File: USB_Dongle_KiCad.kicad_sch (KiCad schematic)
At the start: 52 parts, among them J1 USB_C_Receptacle_USB2.0, J2 Conn SWD 02x05, J3 DM3BT-DSF-PEJS, SW1 PCM12SMTR, SW2 KMR223G LFG, U1 AMS1117-3.3, U2 STULPI01A, U3 USBULC6-2M6, U4 ESDA14V2-2BF3, U5 STM32F730R8Tx, Y1 3225 SMD Oscillator, Y2 24MHz / 10pF / 20ppm

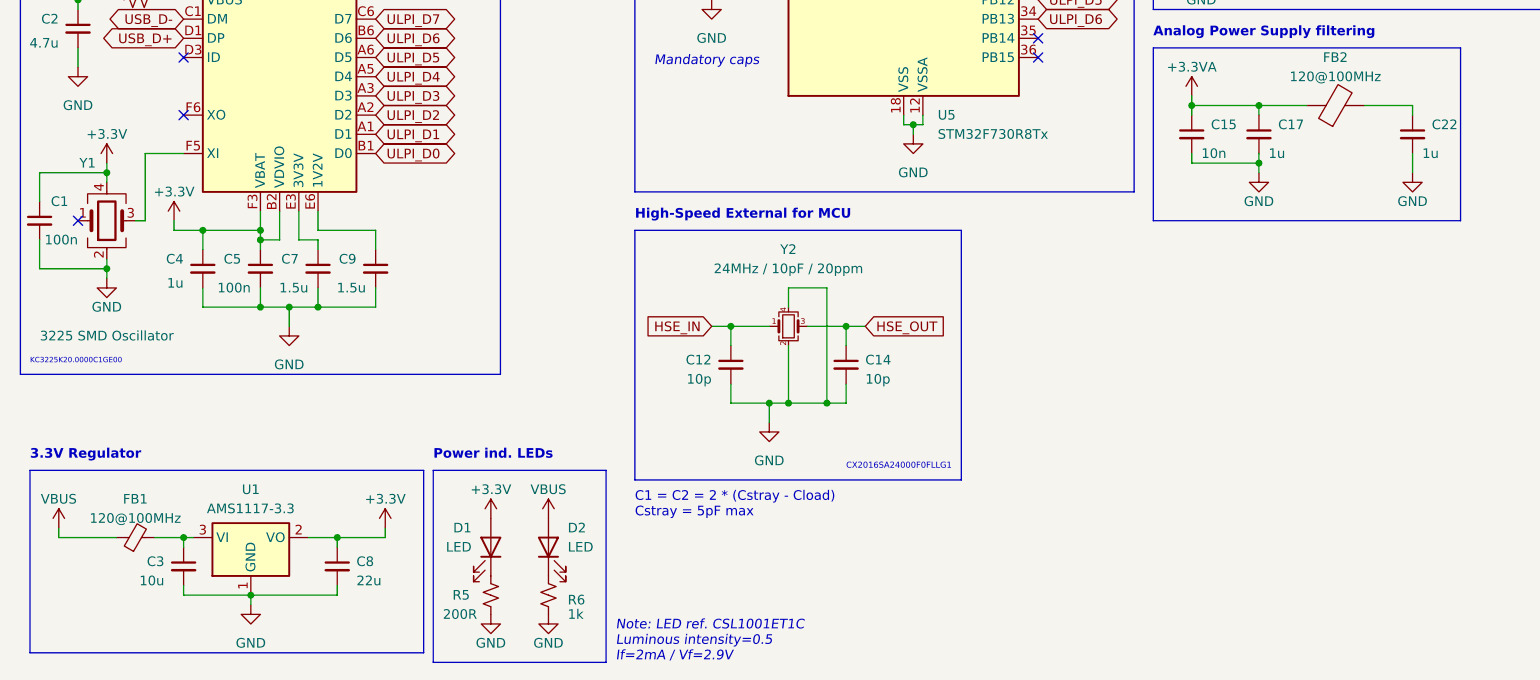
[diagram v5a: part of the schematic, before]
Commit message: Assigned footprints to symbols
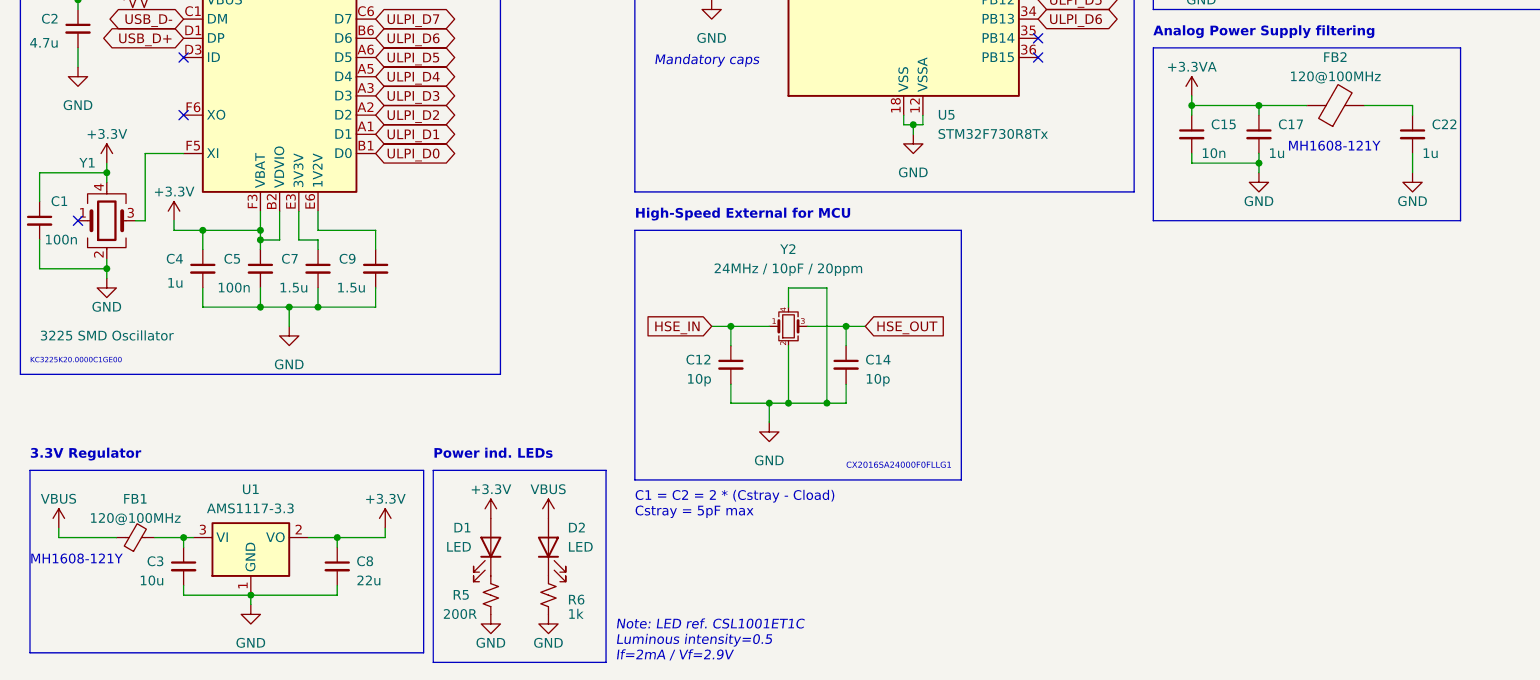
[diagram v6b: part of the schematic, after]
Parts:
- C1, C10, C11, C12, C13, C14, C15, C18, C19, C20, C21, C23, C24, C26, C27, C5: footprint (none) -> Capacitor_SMD:C_0603_1608Metric
- C16, C17, C2, C22, C25, C3, C4, C6, C7, C8, C9: footprint (none) -> Capacitor_SMD:C_0805_2012Metric
- FB1, FB2: footprint (none) -> Inductor_SMD:L_0603_1608Metric
- J1: footprint (none) -> Connector_USB:USB_C_Receptacle_GCT_USB4105-xx-A_16P_TopMnt_Horizontal
- J2: footprint (none) -> Connector_PinHeader_2.54mm:PinHeader_2x05_P2.54mm_Vertical
- R1, R2, R3, R4, R5, R6, R7, R8, R9: footprint (none) -> Resistor_SMD:R_0603_1608Metric
- U3: footprint MICROQFN6_1P45X1_STM -> fplibs:MICROQFN6_1P45X1_STM
- U4: footprint BGA_4V2-2BF3_STM -> fplibs:BGA_4V2-2BF3_STM
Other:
- note added: "MH1608-121Y"

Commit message: Created layout
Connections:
- net USBC_D+: now reaches J1.A6 (D+), J1.B6 (D+), U3.3
- net USBC_D-: now reaches J1.A7 (D-), J1.B7 (D-), U3.1
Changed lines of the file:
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@@
     (effects (font (size 1.27 1.27) (thickness 0.254) bold) (justify left bottom))
+  )
+  (label "USBC_D+" (at 45.72 45.72 0) (fields_autoplaced)
+    (effects (font (size 1.27 1.27)) (justify left bottom))
+  )
+  (label "USBC_D-" (at 45.72 40.64 0) (fields_autoplaced)
+    (effects (font (size 1.27 1.27)) (justify left bottom))
   )
   (global_label "SWDIO" (shape input) (at 191.77 29.21 0) (fields_autoplaced)
@@
     )
     (property "Value" "GND" (at 48.26 43.18 90)
-      (effects (font (size 1.27 1.27)))
+      (effects (font (size 1.27 1.27)) hide)
     )
     (property "Footprint" "" (at 53.34 43.18 0)

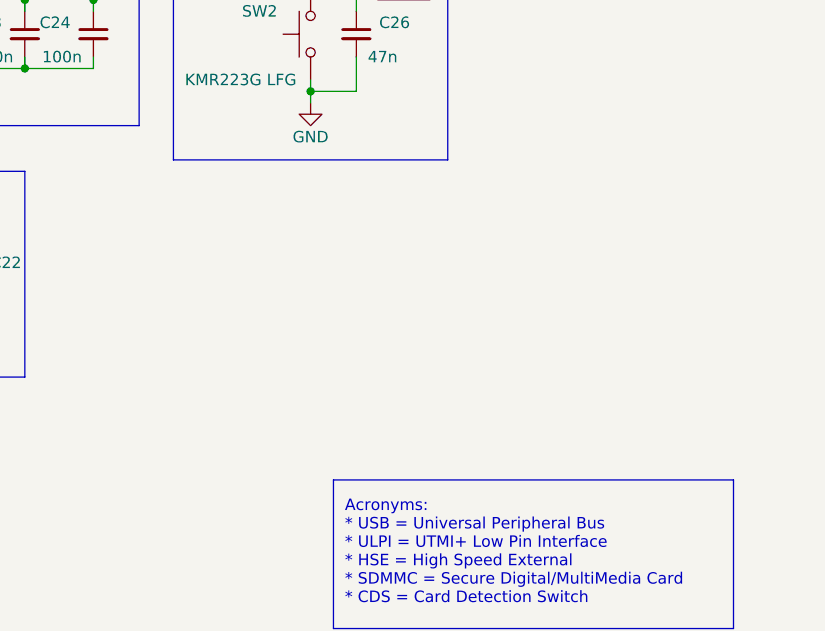
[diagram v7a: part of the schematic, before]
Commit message: Update: Routing of high speed tracks
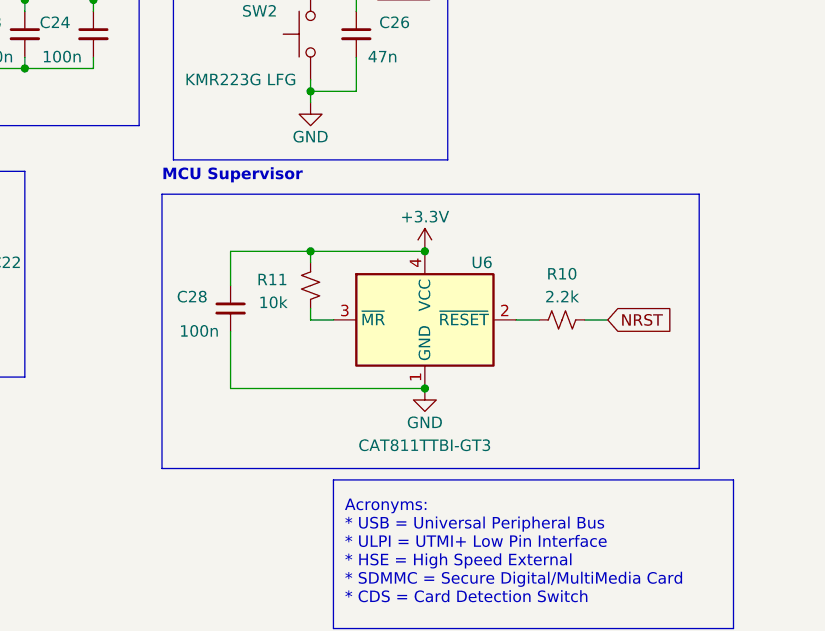
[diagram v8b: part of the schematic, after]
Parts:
- added C28: 100n, Capacitor_SMD:C_0603_1608Metric, symbol Device:C_Small
- added R10: 2.2k, Resistor_SMD:R_0603_1608Metric, symbol Device:R_Small_US
- added R11: 10k, Resistor_SMD:R_0603_1608Metric, symbol Device:R_Small_US
- added U6: CAT811TTBI-GT3, Package_TO_SOT_SMD:SOT-143, symbol Power_Supervisor:CAT811TTBI-GT3
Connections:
- net +3.3V: now also C28.1, R11.1, U6.4 (VCC)
- net GND: now also C28.2, U6.1 (GND)
- net NRST: now also R10.2
- new net: R10.1, U6.2 (~{RESET})
- new net: R11.2, U6.3 (~{MR})
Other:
- note added: "MCU Supervisor"
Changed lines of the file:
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@@
   (junction (at 187.96 95.25) (diameter 0) (color 0 0 0 0)
   )
+  (junction (at 236.22 123.19) (diameter 0) (color 0 0 0 0)
+  )
   (junction (at 38.1 138.43) (diameter 0) (color 0 0 0 0)
   )
@@
   (junction (at 212.09 95.25) (diameter 0) (color 0 0 0 0)
   )
+  (junction (at 248.92 138.43) (diameter 0) (color 0 0 0 0)
+  )
   (junction (at 236.22 105.41) (diameter 0) (color 0 0 0 0)
   )
@@
   (junction (at 177.8 129.54) (diameter 0) (color 0 0 0 0)
   )
+  (junction (at 248.92 123.19) (diameter 0) (color 0 0 0 0)
+  )
   (junction (at 25.4 130.81) (diameter 0) (color 0 0 0 0)
   )
@@
     (stroke (width 0) (type default))
   )
+  (wire (pts (xy 227.33 123.19) (xy 236.22 123.19))
+    (stroke (width 0) (type default))
+  )
   (wire (pts (xy 135.89 29.21) (xy 135.89 27.94))
     (stroke (width 0) (type default))
@@
     (stroke (width 0) (type default))
   )
+  (wire (pts (xy 227.33 138.43) (xy 248.92 138.43))
+    (stroke (width 0) (type default))
+  )
   (wire (pts (xy 133.35 124.46) (xy 132.08 124.46))
     (stroke (width 0) (type default))
@@
     (stroke (width 0) (type default))
   )
+  (wire (pts (xy 227.33 127) (xy 227.33 123.19))
+    (stroke (width 0) (type default))
+  )
   (wire (pts (xy 123.19 158.75) (xy 123.19 161.29))
     (stroke (width 0) (type default))
@@
     (stroke (width 0) (type default))
   )
+  (wire (pts (xy 266.7 130.81) (xy 269.24 130.81))
+    (stroke (width 0) (type default))
+  )
   (wire (pts (xy 115.57 148.59) (xy 115.57 146.05))
     (stroke (width 0) (type default))
@@
     (stroke (width 0) (type default))
   )
+  (wire (pts (xy 227.33 132.08) (xy 227.33 138.43))
+    (stroke (width 0) (type default))
+  )
   (wire (pts (xy 133.35 27.94) (xy 130.81 27.94))
     (stroke (width 0) (type default))
@@
     (stroke (width 0) (type default))
   )
+  (wire (pts (xy 236.22 123.19) (xy 236.22 124.46))
+    (stroke (width 0) (type default))
+  )
   (wire (pts (xy 179.07 95.25) (xy 170.18 95.25))
     (stroke (width 0) (type default))
@@
     (stroke (width 0) (type default))
   )
+  (wire (pts (xy 259.08 130.81) (xy 261.62 130.81))
+    (stroke (width 0) (type default))
+  )
   (wire (pts (xy 125.73 26.67) (xy 125.73 27.94))
     (stroke (width 0) (type default))
@@
     (stroke (width 0) (type default))
   )
+  (wire (pts (xy 238.76 130.81) (xy 236.22 130.81))
+    (stroke (width 0) (type default))
+  )
   (wire (pts (xy 45.72 45.72) (xy 45.72 46.99))
     (stroke (width 0) (type default))
@@
     (stroke (width 0) (type default))
   )
+  (wire (pts (xy 236.22 130.81) (xy 236.22 129.54))
+    (stroke (width 0) (type default))
+  )
   (wire (pts (xy 60.96 138.43) (xy 60.96 140.97))
     (stroke (width 0) (type default))
@@
     (stroke (width 0) (type default))
   )
+  (wire (pts (xy 248.92 123.19) (xy 236.22 123.19))
+    (stroke (width 0) (type default))
+  )
   (wire (pts (xy 76.2 52.07) (xy 76.2 54.61))
     (stroke (width 0) (type default))
@@
     (fill (type none))
   )
+  (rectangle (start 219.71 116.84) (end 279.4 147.32)
+    (stroke (width 0) (type default))
+    (fill (type none))
+  )
   (rectangle (start 212.09 17.78) (end 270.51 72.39)
     (stroke (width 0) (type default))
@@
     (effects (font (size 1.27 1.27)) (justify left bottom))
   )
+  (text "MCU Supervisor" (at 219.71 115.57 0)
+    (effects (font (size 1.27 1.27) (thickness 0.254) bold) (justify left bottom))
+  )
   (text "3.3V Regulator" (at 15.24 168.91 0)
     (effects (font (size 1.27 1.27) (thickness 0.254) bold) (justify left bottom))
@@
     )
   )
+  (global_label "NRST" (shape input) (at 269.24 130.81 0) (fields_autoplaced)
+    (effects (font (size 1.27 1.27)) (justify left))
+    (property "Intersheetrefs" "${INTERSHEET_REFS}" (at 276.9234 130.81 0)
+      (effects (font (size 1.27 1.27)) (justify left) hide)
+    )
+  )
   (global_label "ULPI_D4" (shape bidirectional) (at 148.59 105.41 0) (fields_autoplaced)
     (effects (font (size 1.27 1.27)) (justify left))
@@
     )
   )
+  (symbol (lib_id "power:+3.3V") (at 248.92 123.19 0) (unit 1)
+    (in_bom yes) (on_board yes) (dnp no) (fields_autoplaced)
+    (property "Reference" "#PWR052" (at 248.92 127 0)
+      (effects (font (size 1.27 1.27)) hide)
+    )
+    (property "Value" "+3.3V" (at 248.92 119.38 0)
+      (effects (font (size 1.27 1.27)))
+    )
+    (property "Footprint" "" (at 248.92 123.19 0)
+      (effects (font (size 1.27 1.27)) hide)
+    )
+    (property "Datasheet" "" (at 248.92 123.19 0)
+      (effects (font (size 1.27 1.27)) hide)
+    )
+    (pin "1")
+    (instances
+      (project "USB_Dongle_KiCad"
+        (path "/2a3da274-5b9d-4a25-a42c-dbae4ce402e8"
+          (reference "#PWR052") (unit 1)
+        )
+      )
+    )
+  )
   (symbol (lib_id "Device:C_Small") (at 52.07 59.69 0) (mirror y) (unit 1)
     (in_bom yes) (on_board yes) (dnp no)
@@
     )
   )
+  (symbol (lib_id "Device:R_Small_US") (at 264.16 130.81 90) (unit 1)
+    (in_bom yes) (on_board yes) (dnp no) (fields_autoplaced)
+    (property "Reference" "R10" (at 264.16 125.73 90)
+      (effects (font (size 1.27 1.27)))
+    )
+    (property "Value" "2.2k" (at 264.16 128.27 90)
+      (effects (font (size 1.27 1.27)))
+    )
+    (property "Footprint" "Resistor_SMD:R_0603_1608Metric" (at 264.16 130.81 0)
+      (effects (font (size 1.27 1.27)) hide)
+    )
+    (property "Datasheet" "~" (at 264.16 130.81 0)
+      (effects (font (size 1.27 1.27)) hide)
+    )
+    (pin "1")
+    (pin "2")
+    (instances
+      (project "USB_Dongle_KiCad"
+        (path "/2a3da274-5b9d-4a25-a42c-dbae4ce402e8"
+          (reference "R10") (unit 1)
+        )
+      )
+    )
+  )
   (symbol (lib_id "MCU_ST_STM32F7:STM32F730R8Tx") (at 130.81 77.47 0) (unit 1)
     (in_bom yes) (on_board yes) (dnp no) (fields_autoplaced)
@@
     )
   )
+  (symbol (lib_id "Power_Supervisor:CAT811TTBI-GT3") (at 248.92 130.81 0) (unit 1)
+    (in_bom yes) (on_board yes) (dnp no)
+    (property "Reference" "U6" (at 255.27 124.46 0)
+      (effects (font (size 1.27 1.27)))
+    )
+    (property "Value" "CAT811TTBI-GT3" (at 248.92 144.78 0)
+      (effects (font (size 1.27 1.27)))
+    )
+    (property "Footprint" "Package_TO_SOT_SMD:SOT-143" (at 251.46 138.43 0)
+      (effects (font (size 1.27 1.27)) (justify left) hide)
+    )
+    (property "Datasheet" "http://www.onsemi.com/pub/Collateral/CAT811-D.PDF" (at 240.03 148.59 0)
+      (effects (font (size 1.27 1.27)) hide)
+    )
+    (pin "1")
+    (pin "2")
+    (pin "3")
+    (pin "4")
+    (instances
+      (project "USB_Dongle_KiCad"
+        (path "/2a3da274-5b9d-4a25-a42c-dbae4ce402e8"
+          (reference "U6") (unit 1)
+        )
+      )
+    )
+  )
   (symbol (lib_id "power:GND") (at 53.34 43.18 270) (unit 1)
     (in_bom yes) (on_board yes) (dnp no)
@@
     )
   )
+  (symbol (lib_id "Device:R_Small_US") (at 236.22 127 0) (mirror y) (unit 1)
+    (in_bom yes) (on_board yes) (dnp no)
+    (property "Reference" "R11" (at 233.68 126.365 0)
+      (effects (font (size 1.27 1.27)) (justify left))
+    )
+    (property "Value" "10k" (at 233.68 128.905 0)
+      (effects (font (size 1.27 1.27)) (justify left))
+    )
+    (property "Footprint" "Resistor_SMD:R_0603_1608Metric" (at 236.22 127 0)
+      (effects (font (size 1.27 1.27)) hide)
+    )
+    (property "Datasheet" "~" (at 236.22 127 0)
+      (effects (font (size 1.27 1.27)) hide)
+    )
+    (pin "1")
+    (pin "2")
+    (instances
+      (project "USB_Dongle_KiCad"
+        (path "/2a3da274-5b9d-4a25-a42c-dbae4ce402e8"
+          (reference "R11") (unit 1)
+        )
+      )
+    )
+  )
   (symbol (lib_id "power:GND") (at 76.2 189.23 0) (unit 1)
     (in_bom yes) (on_board yes) (dnp no)
@@
     )
   )
+  (symbol (lib_id "Device:C_Small") (at 227.33 129.54 0) (unit 1)
+    (in_bom yes) (on_board yes) (dnp no)
+    (property "Reference" "C28" (at 224.79 128.27 0)
+      (effects (font (size 1.27 1.27)) (justify right))
+    )
+    (property "Value" "100n" (at 226.06 132.08 0)
+      (effects (font (size 1.27 1.27)) (justify right))
+    )
+    (property "Footprint" "Capacitor_SMD:C_0603_1608Metric" (at 227.33 129.54 0)
+      (effects (font (size 1.27 1.27)) hide)
+    )
+    (property "Datasheet" "~" (at 227.33 129.54 0)
+      (effects (font (size 1.27 1.27)) hide)
+    )
+    (pin "1")
+    (pin "2")
+    (instances
+      (project "USB_Dongle_KiCad"
+        (path "/2a3da274-5b9d-4a25-a42c-dbae4ce402e8"
+          (reference "C28") (unit 1)
+        )
+      )
+    )
+  )
   (symbol (lib_id "Device:C_Small") (at 113.03 102.87 0) (unit 1)
     (in_bom yes) (on_board yes) (dnp no)
@@
         )
       )
+    )
+  )
+  (symbol (lib_id "power:GND") (at 248.92 138.43 0) (unit 1)
+    (in_bom yes) (on_board yes) (dnp no)
+    (property "Reference" "#PWR051" (at 248.92 144.78 0)
+      (effects (font (size 1.27 1.27)) hide)
+    )
+    (property "Value" "GND" (at 248.92 142.24 0)
+      (effects (font (size 1.27 1.27)))
+    )
+    (property "Footprint" "" (at 248.92 138.43 0)
+      (effects (font (size 1.27 1.27)) hide)
+    )
+    (property "Datasheet" "" (at 248.92 138.43 0)
+      (effects (font (size 1.27 1.27)) hide)
+    )
+    (pin "1")
+    (instances
+      (project "USB_Dongle_KiCad"
+        (path "/2a3da274-5b9d-4a25-a42c-dbae4ce402e8"
+          (reference "#PWR051") (unit 1)
+        )
+      )
